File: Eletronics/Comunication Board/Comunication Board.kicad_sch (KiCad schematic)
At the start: 29 parts, among them K1 RELE, T1 AMS1117/3V3, U1 ESP32-S3-WROOM-1-N8R2, U2 BATERIA, U3 MAX17048G

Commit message: Comunication Board edit
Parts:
- added C10, C9: 1 uF, Capacitor_SMD:C_0603_1608Metric, symbol Device:C_Polarized
- added D1: 1N4007, Diode_SMD:D_SMA, symbol Diode:1N4007
- added J1: USB, Connector_USB:USB_Micro-B_Amphenol_10118194_Horizontal, symbol Connector:USB_B_Micro
- added J2: Conn_01x04_Female, symbol Connector:Conn_01x04_Female
- added J3: Conn_01x03_Female, Connector_PinSocket_2.54mm:PinSocket_1x03_P2.54mm_Vertical, symbol Connector:Conn_01x03_Female
- added R10, R9: 100 Ω, Resistor_SMD:R_0603_1608Metric, symbol Device:R_Small
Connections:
- net AnyGPIO is gone; now on net GPIO40: U3.5 (~{ALERT})
- net +5V: now also D1.1 (K)
- net GNDREF: now also C10.2, C9.2, J1.5 (GND), J1.6 (Shield), J3.1 (Pin_1)
- net USB_D-: now reaches U1.13 (IO19)
- net USB_D-: now also R10.1
- net USB_D+: now reaches U1.14 (IO20)
- net USB_D+: now also R9.1
- net SPI_CS: now reaches U1.18 (IO10)
- net SPI_CS: now also J2.1 (Pin_1)
- net SPI_MOSI: now reaches U1.19 (IO11)
- net SPI_MOSI: now also J2.2 (Pin_2)
- net SPI_CLK: now reaches U1.20 (IO12)
- net SPI_CLK: now also J2.3 (Pin_3)
- net SPI_MISO: now reaches U1.21 (IO13)
- net SPI_MISO: now also J2.4 (Pin_4)
- net GPIO45: now reaches U1.26 (IO45)
- net GPIO45: now also K1.NC
- net GPIO40: now reaches U1.33 (IO40)
- net GPIO42: now reaches U1.35 (IO42)
- net GPIO42: now also BZ1.1 (-)
- net RXD0: now reaches U1.36 (RXD0)
- net RXD0: now also J3.3 (Pin_3)
- net TXD0: now reaches U1.37 (TXD0)
- net TXD0: now also J3.2 (Pin_2)
- net GPIO5: now reaches U1.5 (IO5)
- net GPIO5: now also R5.1
- net GPIO6: now reaches U1.6 (IO6)
- net GPIO6: now also R1.1
- net GPIO7: now reaches U1.7 (IO7)
- net GPIO7: now also R6.1
- removed net GPIO: BZ1.1 (-), K1.NC, R1.1, R5.1, R6.1
- new net: C10.1, J1.2 (D-), R10.2
- new net: D1.2 (A), J1.1 (VBUS)
- new net: C9.1, J1.3 (D+), R9.2
- no-connect marks 3 -> 23
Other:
- note added: "Entrada reserva programação"
- note added: "LEDS"
- note added: "SPI"
- note removed: "LEDS - Entrada será escolhida posteriormente"
- moved on the sheet: BZ1, C1, C2, C3, C4, C5, C8, K1, L1, POWER1, R2, R3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

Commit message: Comunication board
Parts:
- added J4: Conn_01x03_Female, Connector_PinSocket_2.54mm:PinSocket_1x03_P2.54mm_Vertical, symbol Connector:Conn_01x03_Female
- BZ1: footprint (none) -> Buzzer_Beeper:Buzzer_12x9.5RM7.6
- J2: footprint (none) -> Connector_PinSocket_2.54mm:PinSocket_1x04_P2.54mm_Vertical
- POWER1: footprint Button_Switch_THT:Nidec_Copal_SH-7010C -> Button_Switch_THT:SW_DIP_SPSTx01_Slide_6.7x4.1mm_W7.62mm_P2.54mm_LowProfile
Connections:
- net GNDREF: now also J4.1 (Pin_1)
- net GPIO42: now also R1.1; no longer BZ1.1 (-)
- net GPIO45: now also BZ1.1 (-); no longer K1.NC
- net I00: now also U1.27 (IO0)
- net RXD0: now also J3.2 (Pin_2); no longer J3.3 (Pin_3)
- net SCL: now also J4.2 (Pin_2)
- net SDA: now also U1.39 (IO1), J4.3 (Pin_3); no longer U1.15 (IO3)
- net TXD0: now also J3.3 (Pin_3); no longer J3.2 (Pin_2)
- net GPIO46: now reaches U1.16 (IO46)
- net GPIO46: now also K1.NC
- net GPIO9: now reaches U1.17 (IO9)
- net GPIO9: now also R5.1
- net GPIO5: no longer names the net of U1.5 (IO5)
- net GPIO5: no longer R5.1
- net GPIO6: no longer names the net of U1.6 (IO6)
- net GPIO6: no longer R1.1
- net GPIO7: no longer names the net of U1.7 (IO7)
- net GPIO7: no longer R6.1
- new net GPIO3: R6.1, U1.15 (IO3)
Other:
- note added: "I2C"

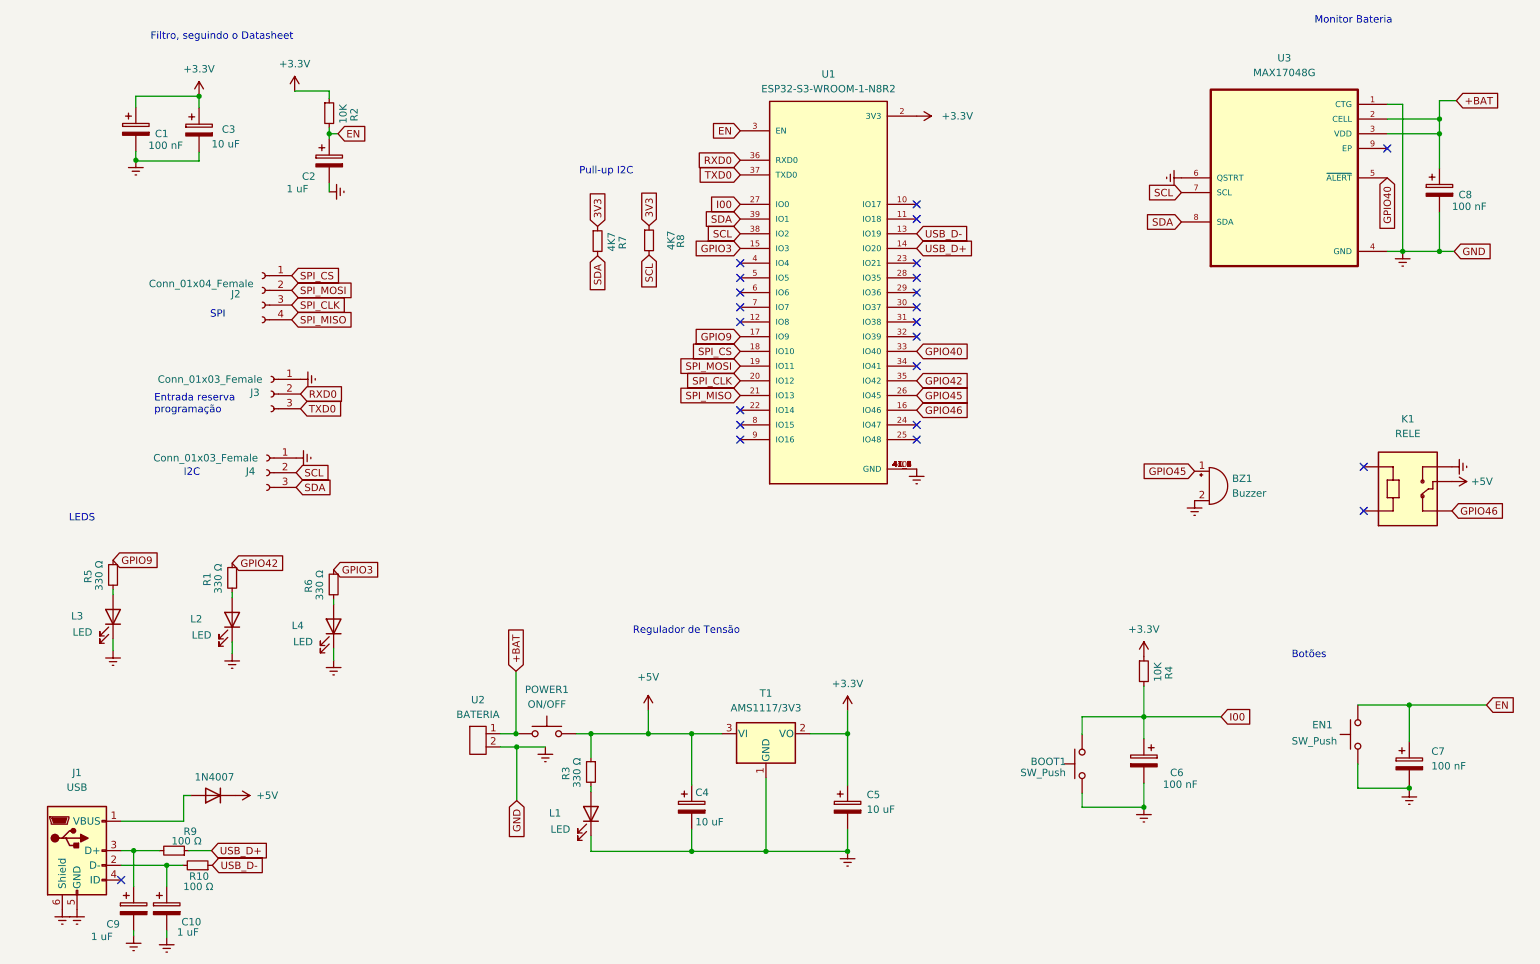
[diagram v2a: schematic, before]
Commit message: Design Commutication Board pcb
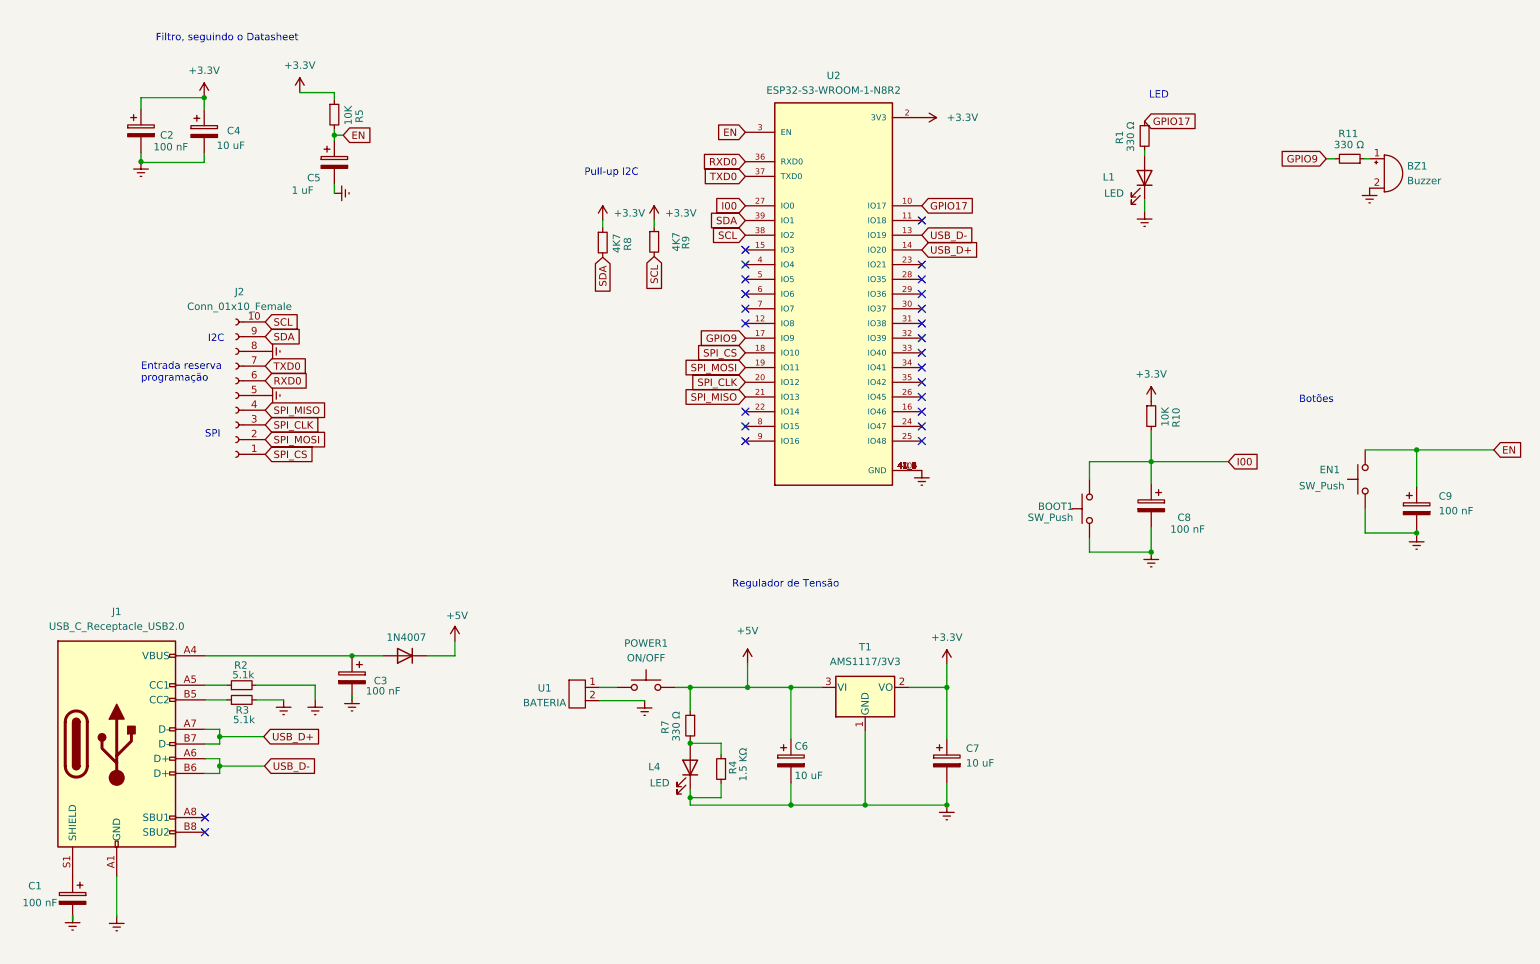
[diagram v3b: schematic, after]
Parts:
- removed C10: 1 uF, Capacitor_SMD:C_0603_1608Metric, symbol Device:C_Polarized
- removed J1: USB, Connector_USB:USB_Micro-B_Amphenol_10118194_Horizontal, symbol Connector:USB_B_Micro
- removed J2: Conn_01x04_Female, Connector_PinSocket_2.54mm:PinSocket_1x04_P2.54mm_Vertical, symbol Connector:Conn_01x04_Female
- removed J3, J4: Conn_01x03_Female, Connector_PinSocket_2.54mm:PinSocket_1x03_P2.54mm_Vertical, symbol Connector:Conn_01x03_Female
- removed K1: RELE, RELAY_SRD-05VDC-SL-C, symbol SRD:SRD-05VDC-SL-C
- removed L2, L3: LED, LED_SMD:LED_0603_1608Metric, symbol Device:LED
- removed R6: 330 Ω, Resistor_SMD:R_0603_1608Metric, symbol Device:R_Small
- removed U1: ESP32-S3-WROOM-1-N8R2, XCVR_ESP32-S3-WROOM-1-N8R2, symbol libs:ESP32-S3-WROOM-1-N8R2
- removed U2: BATERIA, Connector_JST:JST_XH_B2B-XH-AM_1x02_P2.50mm_Vertical, symbol New_Library:BATERIA
- removed U3: MAX17048G, SON50P200X200X80-9N, symbol MAX17048:MAX17048G
- added J1: USB_C_Receptacle_USB2.0, c:USB_C_Receptacle_HRO_TYPE-C-31-M-12, symbol Connector:USB_C_Receptacle_USB2.0
- added J2: Conn_01x10_Female, Connector_IDC:IDC-Header_2x05_P2.54mm_Vertical, symbol Connector:Conn_01x10_Female
- added R11: 330 Ω, Resistor_SMD:R_0603_1608Metric, symbol Device:R_Small
- added U1: BATERIA, Connector_JST:JST_XH_B2B-XH-AM_1x02_P2.50mm_Vertical, symbol New_Library:BATERIA
- added U2: ESP32-S3-WROOM-1-N8R2, XCVR_ESP32-S3-WROOM-1-N8R2, symbol libs:ESP32-S3-WROOM-1-N8R2
- C2, C9: value 1 uF -> 100 nF
- C3: value 10 uF -> 100 nF
- C5: value 10 uF -> 1 uF
- C6, C7: value 100 nF -> 10 uF
- R10: value 100 Ω -> 10K
- R2: value 10K -> 5.1k; LCSC (none) -> C163928
- R3: value 330 Ω -> 5.1k; LCSC (none) -> C163928
- R4: value 10K -> 1.5 KΩ
- R5: value 330 Ω -> 10K
- R7: value 4K7 -> 330 Ω
- R9: value 100 Ω -> 4K7
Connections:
- net +3.3V: now also C2.1, C4.1, C7.1, R10.1, R5.1, R8.1, R9.1, U2.2 (3V3); no longer C1.1, C3.1, C5.1, R2.1, R4.1
- net +5V: now also C6.1, R7.1; no longer C4.1, R3.1
- net EN: now also C5.1, C9.1, R5.2, U2.3 (EN); no longer C2.1, C7.1, R2.2
- net GNDREF: now also R2.2, R3.2, R4.2, J1.A1 (GND), J1.A12 (GND), J1.B1 (GND), J1.B12 (GND), J2.5 (Pin_5), J2.8 (Pin_8), U1.2, U2.1 (GND), U2.40 (GND), U2.41_1 (GND), U2.41_2 (GND), U2.41_3 (GND), U2.41_4 (GND), U2.41_5 (GND), U2.41_6 (GND), U2.41_7 (GND), U2.41_8 (GND), U2.41_9 (GND)
- net GPIO9: now also R11.2, U2.17 (IO9); no longer R5.1
- net I00: now also C8.1, R10.2, U2.27 (IO0); no longer C6.1, R4.2
- net RXD0: now also J2.6 (Pin_6), U2.36 (RXD0)
- net SCL: now also R9.2, J2.10 (Pin_10), U2.38 (IO2); no longer R8.2
- net SDA: now also R8.2, J2.9 (Pin_9), U2.39 (IO1); no longer R7.2
- net SPI_CLK: now also J2.3 (Pin_3), U2.20 (IO12)
- net SPI_CS: now also J2.1 (Pin_1), U2.18 (IO10)
- net SPI_MISO: now also J2.4 (Pin_4), U2.21 (IO13)
- net SPI_MOSI: now also J2.2 (Pin_2), U2.19 (IO11)
- net TXD0: now also J2.7 (Pin_7), U2.37 (TXD0)
- net USB_D+: now also J1.A7 (D-), J1.B7 (D-), U2.14 (IO20); no longer R9.1
- net USB_D-: now also J1.A6 (D+), J1.B6 (D+), U2.13 (IO19); no longer R10.1
- net at D1.2 (A): now also C3.1, J1.A4 (VBUS), J1.A9 (VBUS), J1.B4 (VBUS), J1.B9 (VBUS)
- net at R1.2: now also L1.2 (A)
- net at L4.2 (A): now also R4.1, R7.2
- net +BAT: no longer names the net of POWER1.1
- net +BAT: now also U1.1; no longer C8.1
- removed net 3V3: R7.1, R8.1
- net GPIO42 renamed GPIO17
- net GPIO17: now also U2.10 (IO17)
- net GPIO45: no longer names the net of BZ1.1 (-)
- net GPIO45: now also R11.1
- new net: J1.B5 (CC2), R3.1
- new net: J1.A5 (CC1), R2.1
- new net: C1.1, J1.S1 (SHIELD)
- no-connect marks 23 -> 25
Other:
- note added: "LED"
- note removed: "LEDS"
- note removed: "Monitor Bateria"

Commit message: Communication board schematic
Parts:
- removed BOOT1, EN1: SW_Push, Button_Switch_SMD:SW_SPST_TL3305A, symbol Switch:SW_Push
- removed BZ1: Buzzer, Buzzer_Beeper:Buzzer_12x9.5RM7.6, symbol Device:Buzzer
- removed C1, C2, C3, C8, C9: 100 nF, Capacitor_SMD:C_0603_1608Metric, symbol Device:C_Polarized
- removed C4, C6, C7: 10 uF, Capacitor_SMD:C_0603_1608Metric, symbol Device:C_Polarized
- removed C5: 1 uF, Capacitor_SMD:C_0603_1608Metric, symbol Device:C_Polarized
- removed D1: 1N4007, Diode_SMD:D_SMA, symbol Diode:1N4007
- removed J1: USB_C_Receptacle_USB2.0, c:USB_C_Receptacle_HRO_TYPE-C-31-M-12, symbol Connector:USB_C_Receptacle_USB2.0
- removed J2: Conn_01x10_Female, Connector_IDC:IDC-Header_2x05_P2.54mm_Vertical, symbol Connector:Conn_01x10_Female
- removed L1, L4: LED, LED_SMD:LED_0603_1608Metric, symbol Device:LED
- removed POWER1: ON/OFF, Button_Switch_THT:SW_DIP_SPSTx01_Slide_6.7x4.1mm_W7.62mm_P2.54mm_LowProfile, symbol Switch:SW_Push
- removed R1, R11, R7: 330 Ω, Resistor_SMD:R_0603_1608Metric, symbol Device:R_Small
- removed R10, R5: 10K, Resistor_SMD:R_0603_1608Metric, symbol Device:R_Small
- removed R2, R3: 5.1k, Resistor_SMD:R_0603_1608Metric, symbol Device:R_Small
- removed R4: 1.5 KΩ, Resistor_SMD:R_0603_1608Metric, symbol Device:R_Small
- removed R8, R9: 4K7, Resistor_SMD:R_0603_1608Metric, symbol Device:R_Small
- removed T1: AMS1117/3V3, Package_TO_SOT_SMD:SOT-223-3_TabPin2, symbol Regulator_Linear:LD1117S33TR_SOT223
- removed U1: BATERIA, Connector_JST:JST_XH_B2B-XH-AM_1x02_P2.50mm_Vertical, symbol New_Library:BATERIA
- removed U2: ESP32-S3-WROOM-1-N8R2, XCVR_ESP32-S3-WROOM-1-N8R2, symbol libs:ESP32-S3-WROOM-1-N8R2
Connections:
- no-connect marks 25 -> 0
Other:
- added sheet Bottons (Bottons.kicad_sch)
- added sheet ESP32_S3 (ESP32_S3.kicad_sch)
- added sheet External (External.kicad_sch)
- added sheet Filter (Filter.kicad_sch)
- added sheet Power (Power.kicad_sch)
- added sheet USB (USB.kicad_sch)
- note removed: "Botões"
- note removed: "Entrada reserva programação"
- note removed: "Filtro, seguindo o Datasheet"
- note removed: "I2C"
- note removed: "LED"
- note removed: "Pull-up I2C"
- note removed: "Regulador de Tensão"
- note removed: "SPI"
